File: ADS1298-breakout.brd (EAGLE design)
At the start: 63.5 x 25.4 mm, 32 parts, among them IC1 ADS1298*PAG*, IC2 TPS73250DBVT, IC3 TPS73233DBVT

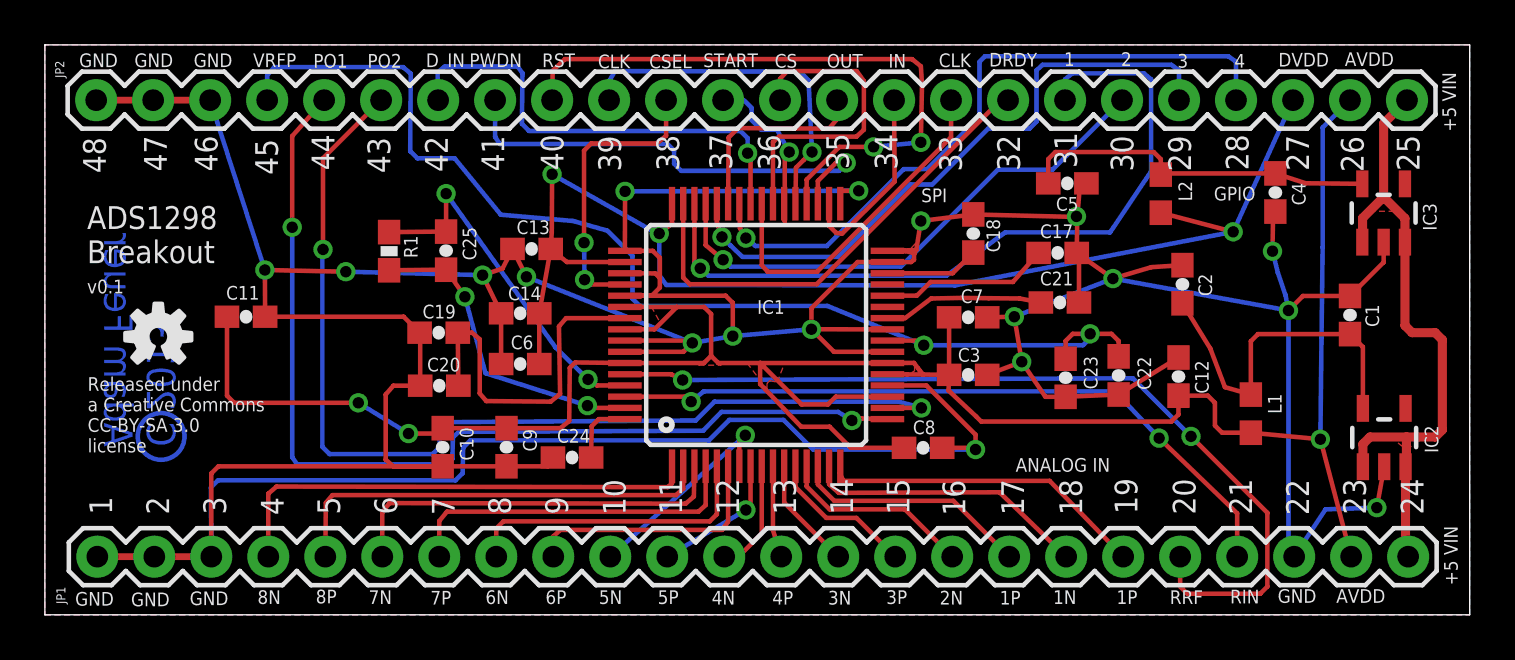
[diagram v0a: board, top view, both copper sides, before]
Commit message: minor cosmetic updates to silkscreen
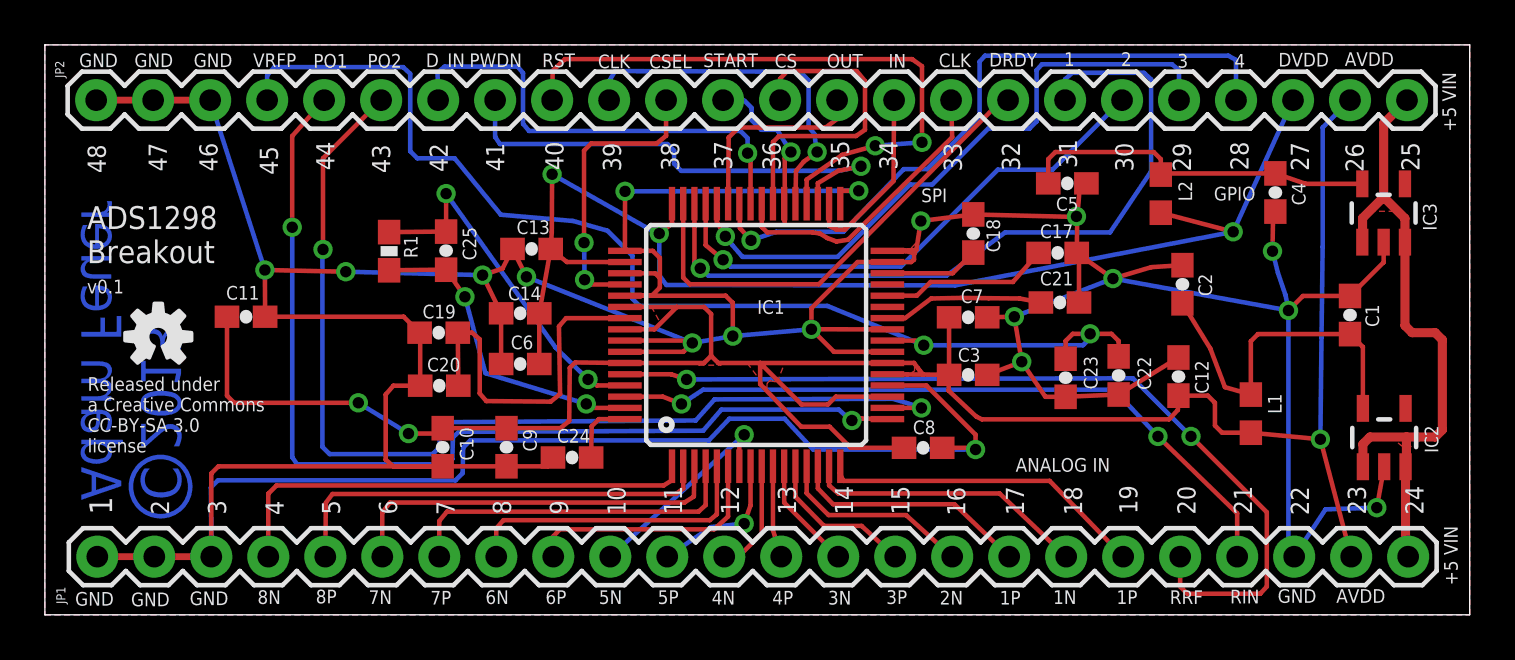
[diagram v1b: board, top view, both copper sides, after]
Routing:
- net SPI_CLK: track 15.4 -> 13.2 mm
- net !PWDN: track 21.1 -> 22.0 mm
